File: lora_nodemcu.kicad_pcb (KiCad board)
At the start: 2 copper layers, 2 parts

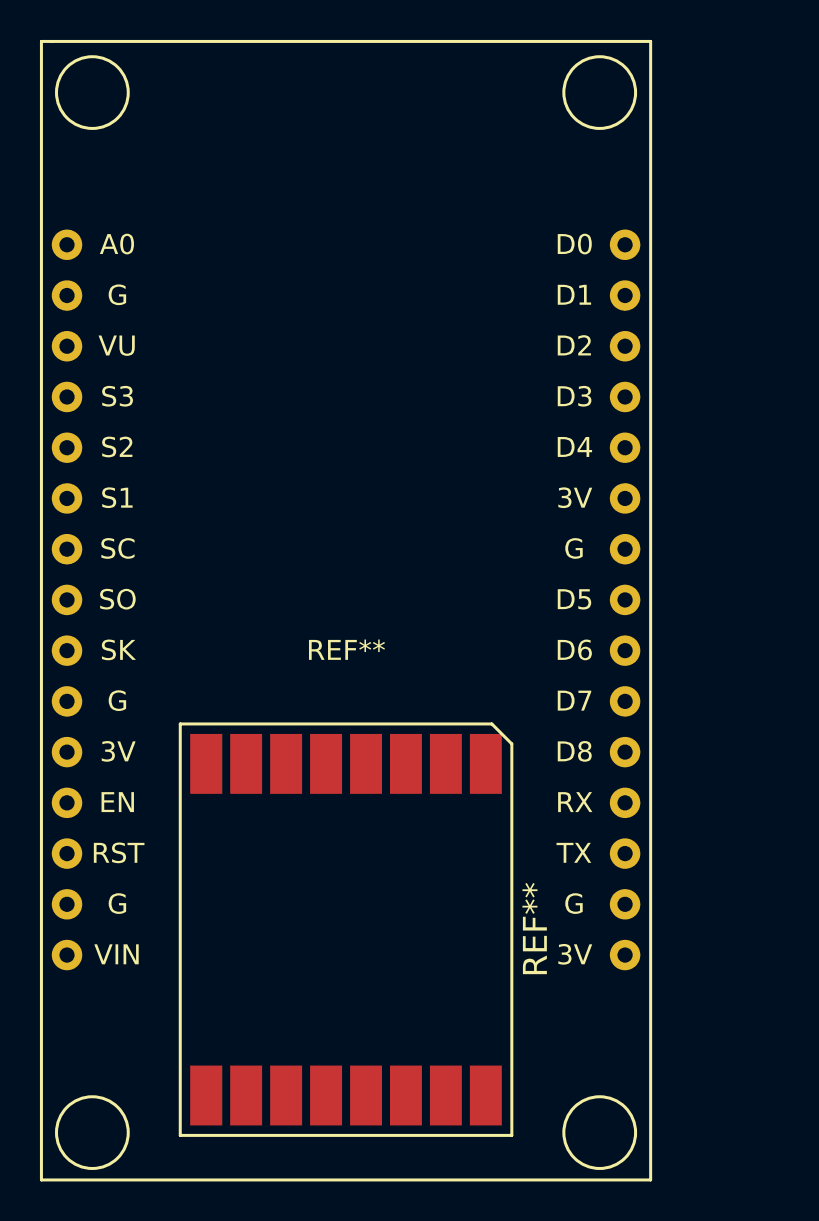
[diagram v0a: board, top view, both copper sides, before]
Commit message: Finalized schematic, first run at board layout.
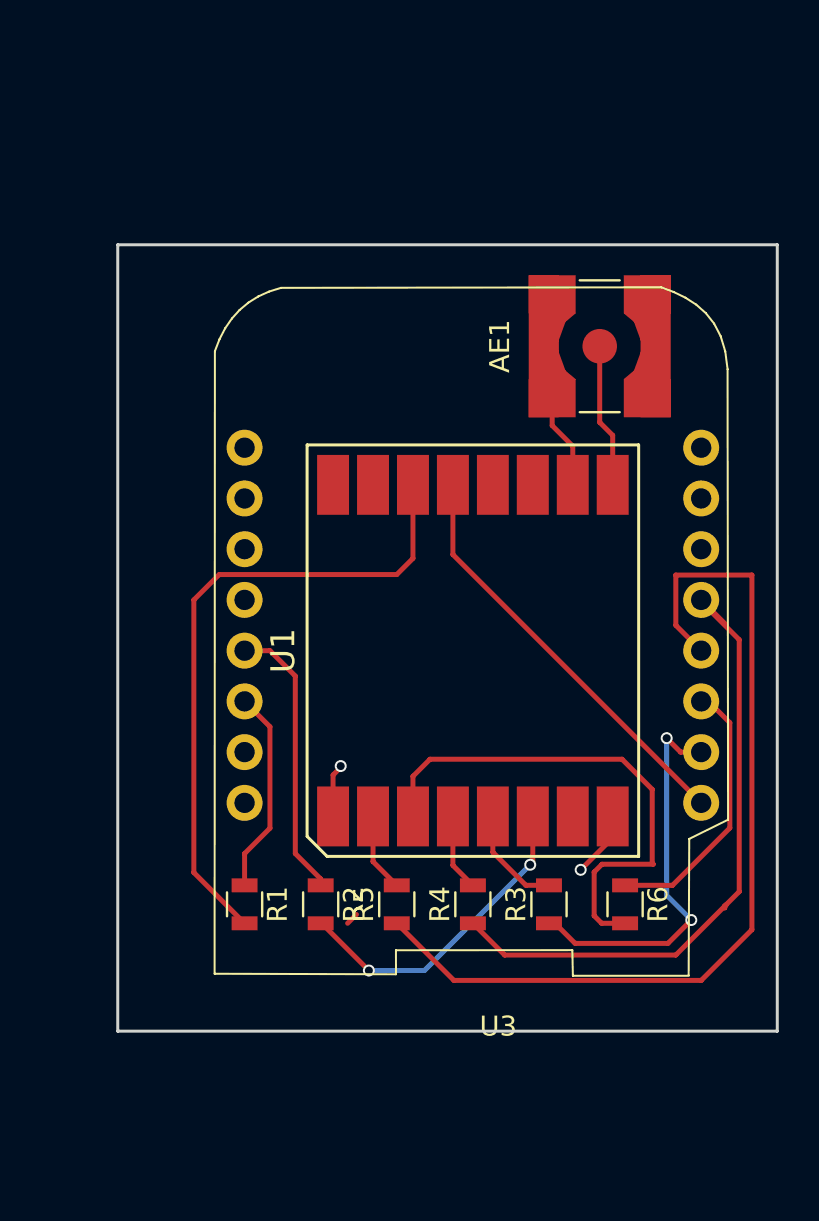
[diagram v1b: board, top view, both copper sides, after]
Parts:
- removed REF**: NodeMCU1.0(12-E), ESP8266:NodeMCU1.0(12-E)
- removed REF**: RFM95, DisasterRadio:RFM95
- added AE1: Ant, Connectors:SMA_SMD_Jack_Straight, F.Cu at (153.7, 74.9)
- added R1: 0k, Resistors_SMD:R_0805, F.Cu at (135.9, 102.9)
- added R2: 0k, Resistors_SMD:R_0805, F.Cu at (139.7, 102.9)
- added R3: 0k, Resistors_SMD:R_0805, F.Cu at (151.1, 102.9)
- added R4: 0k, Resistors_SMD:R_0805, F.Cu at (147.3, 102.9)
- added R5: 0k, Resistors_SMD:R_0805, F.Cu at (143.5, 102.9)
- added R6: 0k, Resistors_SMD:R_0805, F.Cu at (154.9, 102.9)
- added U1: RFM95, DisasterRadio:RFM95, F.Cu at (147.3, 90.2)
- added U3: WeMos_mini, DisasterRadio:D1_mini_Hat, F.Cu at (147.3, 90.2)
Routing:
- net /MISO: track 0.00 -> 45.9 mm
- net /SCK: track 0.00 -> 32.8 mm
- net Net-(R1-Pad2): track 0.00 -> 32.8 mm
- net Net-(R6-Pad2): track 0.00 -> 25.7 mm
- net +3V3: track 0.00 -> 21.1 mm
- net /SS: track 0.00 -> 19.7 mm, vias 0 -> 2
- net Net-(AE1-Pad2): track 0.00 -> 19.0 mm
- net Net-(R2-Pad2): track 0.00 -> 16.1 mm, vias 0 -> 2
- net Net-(R2-Pad1): track 0.00 -> 14.1 mm
- net /MOSI: track 0.00 -> 13.6 mm
- net Net-(R1-Pad1): track 0.00 -> 10.3 mm
- net Net-(AE1-Pad1): track 0.00 -> 7.21 mm
- net GND: track 0.00 -> 6.02 mm, vias 0 -> 2
- net Net-(R3-Pad2): track 0.00 -> 5.29 mm
- net Net-(R5-Pad2): track 0.00 -> 3.94 mm
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- added copper zone on In1.Cu, net GND
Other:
- board outline added: 33 x 39.4 mm
- copper layers 2 -> 4

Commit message: Relayed out board.
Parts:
- AE1: value Ant -> Antenna_Shield
- moved AE1 75.2 mm to (156.6, 150.1), turned to 270 degrees
- moved U1 46.3 mm to (163.6, 133.5), turned to 180 degrees
- moved U3 39.6 mm to (163.4, 126.4)
- moved R5 32.0 mm to (170.6, 119.8), turned to 180 degrees
- moved R1 28.2 mm to (161.5, 114.6), turned to 0 degrees
- moved R4 25.5 mm to (166.5, 119.7), turned to 180 degrees
- moved R2 20.3 mm to (156.6, 114.2), turned to 0 degrees
- moved R6 20.0 mm to (171.0, 114.8), turned to 180 degrees
- moved R3 19.7 mm to (167.0, 114.7), turned to 180 degrees
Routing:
- net /MISO: track 45.9 -> 8.55 mm, vias 0 -> 2
- net /SCK: track 32.8 -> 9.89 mm, vias 0 -> 2
- net Net-(R6-Pad2): track 25.7 -> 11.8 mm
- net Net-(R1-Pad1): track 10.3 -> 18.6 mm
- net Net-(AE1-Pad2): track 19.0 -> 11.1 mm
- net /SS: track 19.7 -> 26.9 mm, vias 2 -> 0
- net Net-(R3-Pad2): track 5.29 -> 11.9 mm
- net Net-(R1-Pad2): track 32.8 -> 29.0 mm, vias 0 -> 2
- net Net-(R2-Pad2): track 16.1 -> 12.7 mm
- net GND: track 6.02 -> 9.01 mm, vias 2 -> 1
- net (no net): track 0.63 -> 2.97 mm, vias 0 -> 1
- net Net-(R4-Pad2): track 3.86 -> 5.93 mm
- net Net-(R5-Pad2): track 3.94 -> 5.79 mm
- net /MOSI: track 13.6 -> 15.4 mm, vias 0 -> 2
- net Net-(AE1-Pad1): track 7.21 -> 8.33 mm
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- removed copper zone on In1.Cu, net GND
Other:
- board outline removed

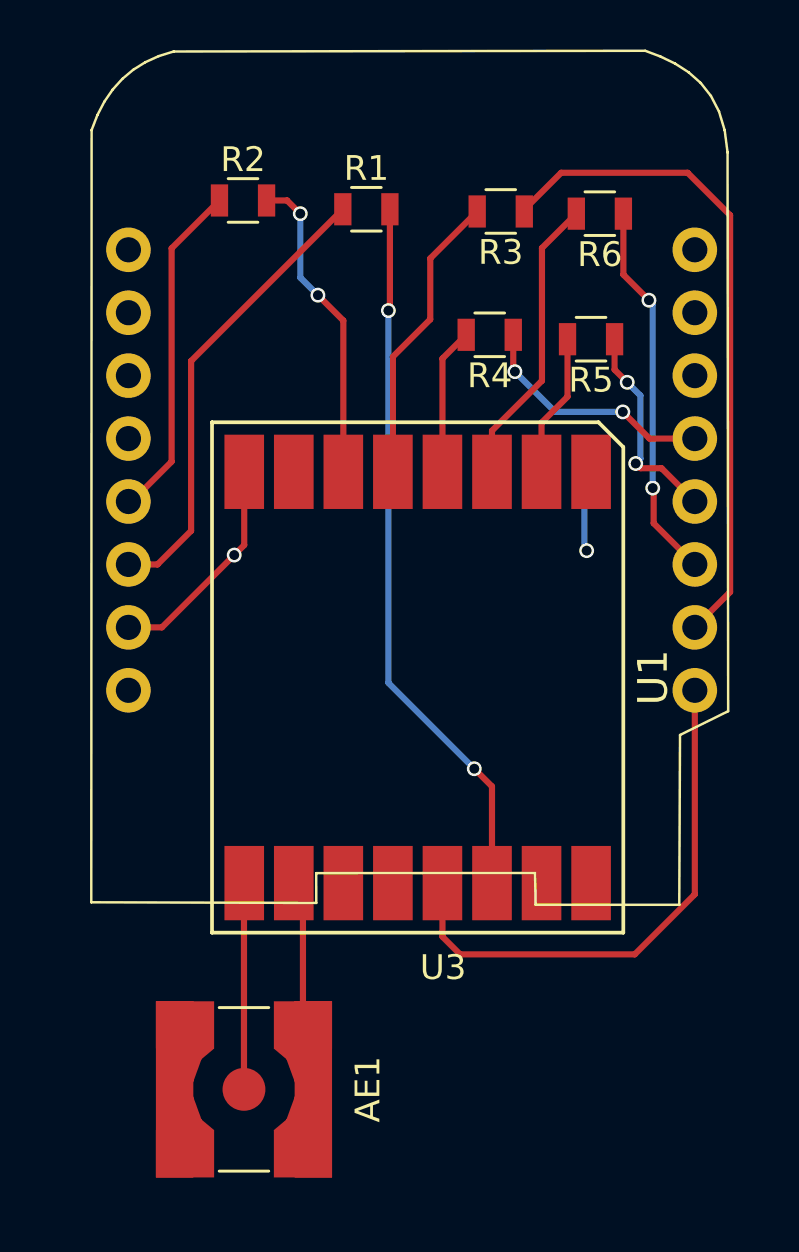
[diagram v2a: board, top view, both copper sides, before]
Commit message: Added cut-out and missing ground connector.
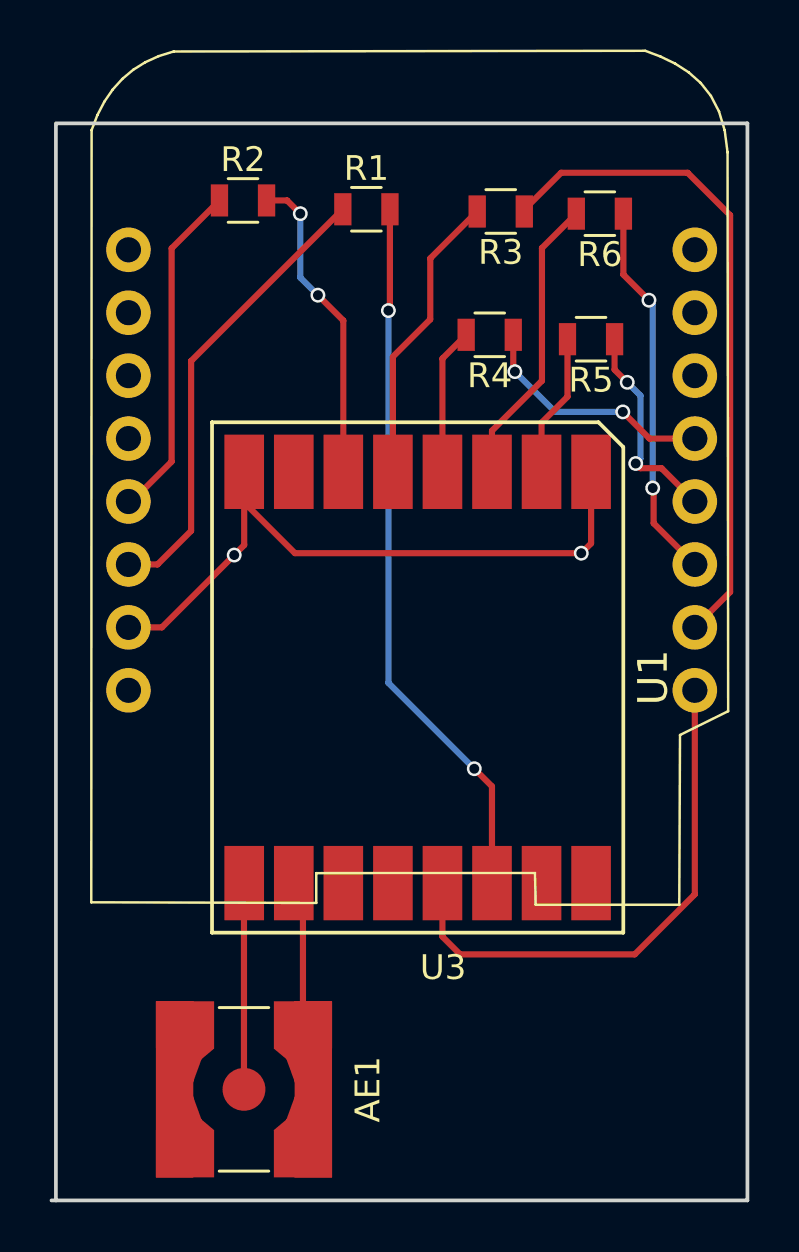
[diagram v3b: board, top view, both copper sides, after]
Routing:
- net GND: track 9.01 -> 28.1 mm, vias 1 -> 2
- net (no net): track 2.97 -> 0.00 mm, vias 1 -> 0
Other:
- board outline added: 28.1 x 43.5 mm
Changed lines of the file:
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@@
   (general
     (links 30)
-    (no_connects 2)
+    (no_connects 1)
     (area 150.1775 106.3625 176.537502 155.956858)
     (thickness 1.2)
-    (drawings 0)
-    (tracks 88)
+    (drawings 4)
+    (tracks 91)
     (zones 0)
     (modules 9)
@@
       (effects (font (size 1 1) (thickness 0.15)))
     )
-    (fp_text value WeMos_mini (at 1.27 -19.05) (layer F.Fab)
+    (fp_text value WeMos_mini (at 0.218306 -16.6849) (layer F.Fab)
       (effects (font (size 1 1) (thickness 0.15)))
     )
@@
       (effects (font (size 1 1) (thickness 0.15)))
     )
-    (fp_text value Antenna_Shield (at 0 5 270) (layer F.Fab)
+    (fp_text value Antenna_Shield (at -1.524 5.08 270) (layer F.Fab)
       (effects (font (size 1 1) (thickness 0.15)))
     )
@@
       (net 16 GND))
   )
-  (segment (start 170.3324 125.4379) (end 170.3324 128.2827) (width 0.25) (layer B.Cu) (net 0))
-  (via (at 170.4213 128.3716) (size 0.6) (drill 0.4) (layers F.Cu B.Cu) (net 0))
-  (segment (start 170.3324 128.2827) (end 170.4213 128.3716) (width 0.25) (layer B.Cu) (net 0))
+  (gr_line (start 149 154.5971) (end 149 111.2139) (angle 90) (layer Edge.Cuts) (width 0.15))
+  (gr_line (start 176.911 154.5971) (end 148.8186 154.5971) (angle 90) (layer Edge.Cuts) (width 0.15))
+  (gr_line (start 176.911 111.125) (end 176.911 154.5971) (angle 90) (layer Edge.Cuts) (width 0.15))
+  (gr_line (start 149 111.125) (end 176.911 111.125) (angle 90) (layer Edge.Cuts) (width 0.15))
   (segment (start 158.971 150.964) (end 158.971 142.1593) (width 0.25) (layer F.Cu) (net 1))
   (segment (start 158.971 142.1593) (end 158.6014 141.7897) (width 0.25) (layer F.Cu) (net 1))
@@
   (segment (start 164.6014 125.1897) (end 164.6014 120.6177) (width 0.25) (layer F.Cu) (net 10))
   (segment (start 164.6014 120.6177) (end 165.5597 119.6594) (width 0.25) (layer F.Cu) (net 10))
-  (segment (start 171.5491 119.8372) (end 171.5491 121.0666) (width 0.25) (layer F.Cu) (net 11) (status 400000))
-  (segment (start 173.444394 125.0442) (end 174.787694 126.3875) (width 0.25) (layer F.Cu) (net 11) (status 800000))
+  (segment (start 171.5491 119.8372) (end 171.5491 121.0666) (width 0.25) (layer F.Cu) (net 11))
+  (segment (start 173.444394 125.0442) (end 174.787694 126.3875) (width 0.25) (layer F.Cu) (net 11))
   (segment (start 172.593 125.0442) (end 173.444394 125.0442) (width 0.25) (layer F.Cu) (net 11))
   (segment (start 172.4025 124.8537) (end 172.593 125.0442) (width 0.25) (layer F.Cu) (net 11))
@@
   (segment (start 168.6179 121.5136) (end 168.6179 116.1567) (width 0.25) (layer F.Cu) (net 14))
   (segment (start 166.6014 123.5301) (end 168.6179 121.5136) (width 0.25) (layer F.Cu) (net 14))
+  (segment (start 156.6014 125.1897) (end 156.6014 126.4262) (width 0.25) (layer F.Cu) (net 16) (status C00000))
+  (segment (start 156.6014 126.4262) (end 158.6484 128.4732) (width 0.25) (layer F.Cu) (net 16) (status 400000))
+  (segment (start 170.6014 128.0772) (end 170.2054 128.4732) (width 0.25) (layer F.Cu) (net 16))
+  (via (at 170.2054 128.4732) (size 0.6) (drill 0.4) (layers F.Cu B.Cu) (net 16))
+  (segment (start 170.6014 125.1897) (end 170.6014 128.0772) (width 0.25) (layer F.Cu) (net 16) (status 400000))
+  (segment (start 158.6484 128.4732) (end 170.2054 128.4732) (width 0.25) (layer F.Cu) (net 16))
   (segment (start 151.927694 131.4675) (end 153.2792 131.4675) (width 0.25) (layer F.Cu) (net 16))
   (segment (start 156.6014 128.1453) (end 156.1973 128.5494) (width 0.25) (layer F.Cu) (net 16))

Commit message: fixed traces, added 3.3v power management
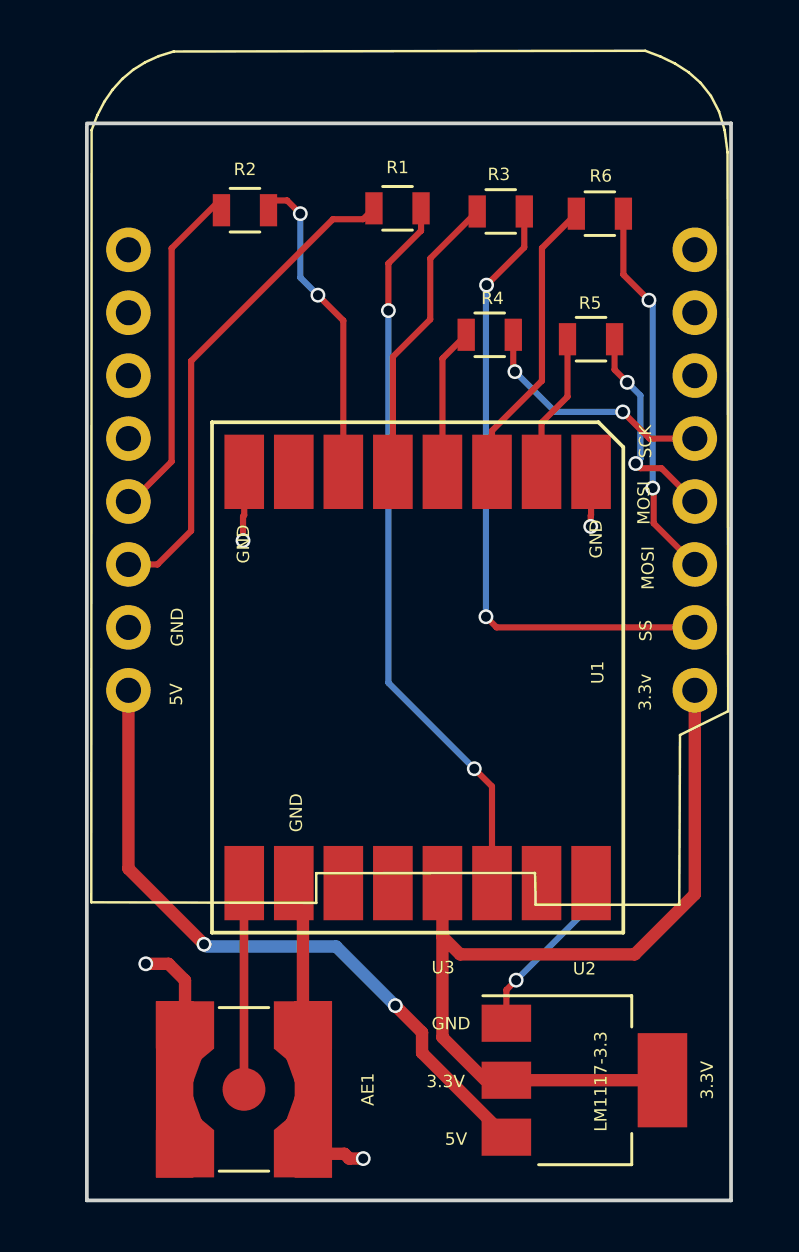
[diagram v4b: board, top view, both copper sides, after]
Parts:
- added U2: LM1117-3.3, TO_SOT_Packages_SMD:SOT-223, F.Cu at (170.3, 149.7)
- AE1: value Antenna_Shield -> Antenna
- moved R1 1.26 mm to (162.8, 114.6)
- moved R2 0.40 mm to (156.6, 114.6)
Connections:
- AE1 pad 2: Net-(AE1-Pad2) -> GND
- U1 pad 10: Net-(AE1-Pad2) -> GND
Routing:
- net +5V: track 0.00 -> 27.4 mm, vias 0 -> 2
- net +3V3: track 21.9 -> 37.7 mm
- net Net-(AE1-Pad2): track 11.1 -> 0.00 mm
- net GND: track 28.1 -> 30.9 mm, vias 2 -> 5
- net Net-(R1-Pad1): track 18.6 -> 19.9 mm
- net /SS: track 26.9 -> 25.7 mm, vias 0 -> 2
- net Net-(R1-Pad2): track 29.0 -> 29.6 mm
- added copper zone on In2.Cu, net +3V3
- added copper zone on In1.Cu, net GND
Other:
- board size 28.1 x 43.5 mm -> 26 x 43.5 mm
- board text added: "3.3V"
- board text added: "3.3v"
- board text added: "5V"
- board text added: "GND"
- board text added: "LM1117-3.3"
- board text added: "MOSI"
- board text added: "SCK"
- board text added: "SS"

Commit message: backup save for prosperity
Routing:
- added copper zone on B.Cu, net GND
- added copper zone on F.Cu, net GND
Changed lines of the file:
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@@
     (links 35)
     (no_connects 0)
-    (area 150.174999 111.049999 176.325001 154.672101)
+    (area 150.174999 107.945765 176.383721 154.872)
     (thickness 1.2)
     (drawings 19)
@@
   (layers
     (0 F.Cu signal)
-    (1 In1.Cu power)
-    (2 In2.Cu power)
-    (31 B.Cu signal)
+    (1 In1.Cu power hide)
+    (2 In2.Cu power hide)
+    (31 B.Cu signal hide)
     (33 F.Adhes user)
     (35 F.Paste user)
@@
   )
   (setup
-    (last_trace_width 0.5)
+    (last_trace_width 0.25)
     (user_trace_width 0.5)
     (trace_clearance 0.2)
@@
     (effects (font (size 0.5 0.5) (thickness 0.1)))
   )
-  (gr_text GND (at 164.9476 147.4597 360) (layer F.SilkS)
+  (gr_text GND (at 164.9476 147.4597) (layer F.SilkS)
     (effects (font (size 0.5 0.5) (thickness 0.1)))
   )
@@
       )
     )
+  )
+  (zone (net 15) (net_name GND) (layer F.Cu) (hatch edge 0.508)
+    (connect_pads (clearance 0.1524))
+    (min_thickness 0.254)
+    (fill yes (arc_segments 16) (thermal_gap 0.508) (thermal_bridge_width 0.508))
+    (polygon
+      (pts
+        (xy 150.3553 111.1504) (xy 176.1363 111.1758) (xy 176.3014 154.6225) (xy 150.2664 154.6225)
+      )
+    )
+  )
+  (zone (net 15) (net_name GND) (layer B.Cu) (hatch edge 0.508)
+    (connect_pads (clearance 0.1524))
+    (min_thickness 0.254)
+    (fill yes (arc_segments 16) (thermal_gap 0.508) (thermal_bridge_width 0.508))
+    (polygon
+      (pts
+        (xy 150.241 111.125) (xy 176.2252 111.1504) (xy 176.2506 154.5717) (xy 150.2537 154.559)
+      )
+    )
+  )
+  (zone (net 0) (net_name "") (layer F.Cu) (hatch edge 0.508)
+    (connect_pads (clearance 0.1524))
+    (min_thickness 0.254)
+    (keepout (tracks allowed) (vias allowed) (copperpour not_allowed))
+    (fill yes (arc_segments 16) (thermal_gap 0.508) (thermal_bridge_width 0.508))
+    (polygon
+      (pts
+        (xy 154.9527 143.5862) (xy 158.5849 143.6243) (xy 159.0167 154.4701) (xy 154.8511 154.4955) (xy 154.9527 143.6116)
+      )
+    )

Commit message: Finalized PCB
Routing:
- net +5V: track 27.4 -> 28.0 mm
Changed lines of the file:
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@@
     (thickness 1.2)
     (drawings 19)
-    (tracks 122)
+    (tracks 123)
     (zones 0)
     (modules 10)
@@
   (layers
     (0 F.Cu signal)
-    (1 In1.Cu power hide)
-    (2 In2.Cu power hide)
-    (31 B.Cu signal hide)
+    (1 In1.Cu power)
+    (2 In2.Cu power)
+    (31 B.Cu signal)
     (33 F.Adhes user)
     (35 F.Paste user)
+    (36 B.SilkS user)
     (37 F.SilkS user)
+    (38 B.Mask user)
     (39 F.Mask user)
     (40 Dwgs.User user)
@@
     (visible_elements FFFFFF7F)
     (pcbplotparams
-      (layerselection 0x00030_80000001)
-      (usegerberextensions false)
+      (layerselection 0x010f0_80000007)
+      (usegerberextensions true)
       (excludeedgelayer true)
       (linewidth 0.100000)
@@
       (outputformat 1)
       (mirror false)
-      (drillshape 1)
+      (drillshape 0)
       (scaleselection 1)
       (outputdirectory ""))
@@
   (segment (start 165.3159 144.6657) (end 172.3644 144.6657) (width 0.5) (layer F.Cu) (net 17))
   (segment (start 164.6014 143.9512) (end 165.3159 144.6657) (width 0.5) (layer F.Cu) (net 17))
+  (segment (start 162.6997 146.7358) (end 163.7792 147.8153) (width 0.5) (layer F.Cu) (net 25))
+  (segment (start 163.7792 147.8153) (end 163.7792 149.5552) (width 0.5) (layer F.Cu) (net 25))
+  (segment (start 163.7792 149.5552) (end 166.2697 152.0457) (width 0.5) (layer F.Cu) (net 25))
+  (segment (start 166.2697 152.0457) (end 167.1824 152.0457) (width 0.5) (layer F.Cu) (net 25))
   (segment (start 151.927694 134.0075) (end 151.927694 141.208894) (width 0.5) (layer F.Cu) (net 25))
-  (segment (start 163.7792 148.6425) (end 167.1824 152.0457) (width 0.5) (layer F.Cu) (net 25))
-  (segment (start 163.7792 147.8153) (end 163.7792 148.6425) (width 0.5) (layer F.Cu) (net 25))
-  (segment (start 162.6997 146.7358) (end 163.7792 147.8153) (width 0.5) (layer F.Cu) (net 25))
   (via (at 162.6997 146.7358) (size 0.6) (drill 0.4) (layers F.Cu B.Cu) (net 25))
   (segment (start 160.3121 144.3482) (end 162.6997 146.7358) (width 0.5) (layer B.Cu) (net 25))
@@
     (polygon
       (pts
-        (xy 154.9527 143.5862) (xy 158.5849 143.6243) (xy 159.0167 154.4701) (xy 154.8511 154.4955) (xy 154.9527 143.6116)
+        (xy 155.8984 143.5862) (xy 157.2835 143.6243) (xy 157.2835 154.4701) (xy 155.8984 154.4955)
       )
     )
